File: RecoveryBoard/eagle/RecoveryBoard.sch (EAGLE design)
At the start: 96 parts, among them Q1 BSS123, Q2 BSS123, Q3 BSS123, Q4 BPR-301, Q5 BPR-301, Q6 MOSFET-PCH-SOT23-6, U1 STM32F042K6, U10 TPS63070, U2 BD62120AEFJ-E2, U3 H11F1SR2M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

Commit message: fixed first round of issues with Rev1.0, and fixed some libraries as well
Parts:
- removed U$6: NHQ103B375T10, R--NHQ103B375T10--Thermistor:NHQ103B375T10
- removed U$8: SI7465DP, Q--Si7465DP--Vishay Power MOSFET with multple S+D leads:SI7465DP
- added Q7: SI7465DP-T1-E3, Q--Si7465DP--Vishay Power MOSFET with multple S+D leads:SI7465DP-T1-E3
- added R5: (no value), R--NHQ103B375T10--Thermistor 10K:NHQ103B375T10
- C22: device oresat-rcl:C-EUC1206 -> oresat-rcl:C-EU0805-A-NOSILK
- R8, R9: value 470 -> 220
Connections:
- net +12V: now also Q7.D; no longer U$8.D
- net 3.3V: now also J2.5; no longer J2.3
- net GND: now also J2.1, R5.P$2; no longer J2.5, U$6.P1
- net LAMOTOR+: now also J2.3; no longer J2.1
- net LAMOTOR-: now also J2.4; no longer J2.2
- net N$16: now also Q7.G; no longer U$8.G
- net N$20: now also R5.P$1; no longer U$6.P2
- net POT_OUT_AN: now also J2.2; no longer J2.4
- net VBAT: now also Q7.S; no longer U$8.S
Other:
- note removed: "MOTOR+"
- note removed: "MOTOR-"
- note removed: "POT out"
- note removed: "POT+"
- note removed: "POT-"
- moved on the sheet: JP4

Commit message: updated board with more test points, rearranged LA pins, and rearannged AI STM32 pins
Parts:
- added TP11, TP12, TP13, TP14, TP15, TP16, TP17, TP5, TP7, TP8: TEST-POINT, Tova:TEST-POINT
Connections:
- net IN1 renamed LA_IN1
- net IN2 renamed LA_IN2
- removed net POT_OUT_AN: J2.2, U1.PA10
- new net LA_POS: J2.2, TP8.1, U1.PA1
- net BATT_READ: now also U1.PB1; no longer U1.PB6
- net CHUTE: now also TP13.1
- net DROGUE: now also TP12.1
- net ISO-CHUTE: now also TP14.1
- net ISO-DROGUE: now also TP15.1
- net N$16: now also TP11.1
- net N$2: now also TP16.1
- net N$5: now also TP17.1
- net SENSOR1: now also TP5.1
- net SENSOR2: now also TP7.1
- net SPKR: now also U1.PA10; no longer U1.PB1
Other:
- moved on the sheet: R8, R9

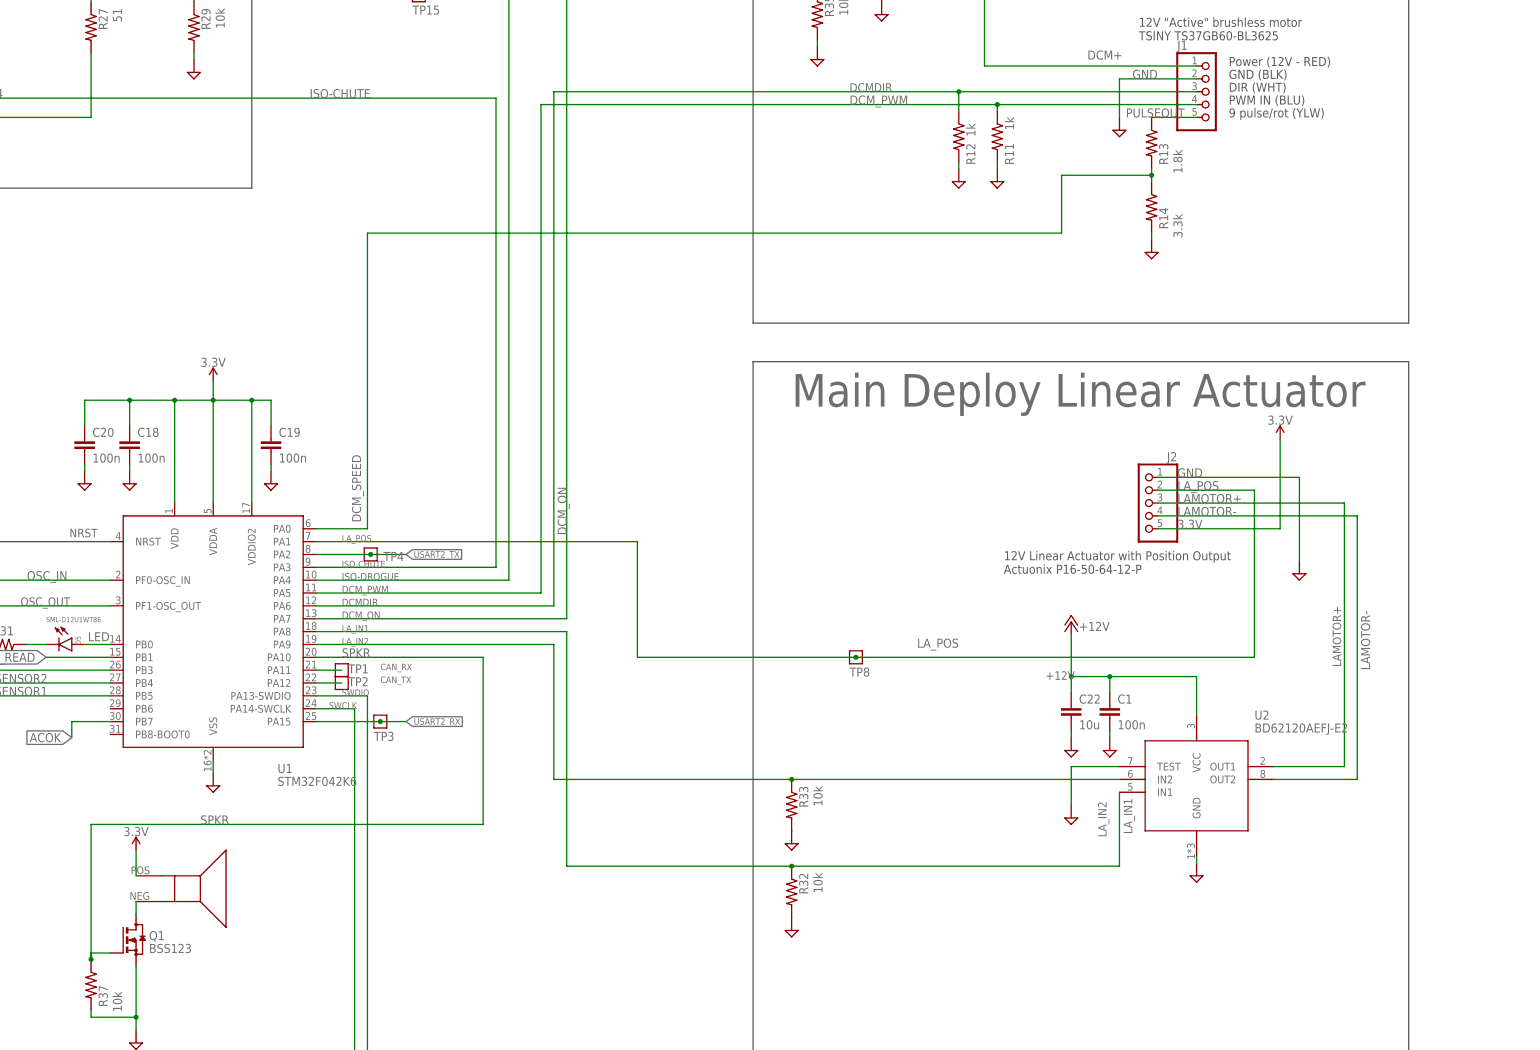
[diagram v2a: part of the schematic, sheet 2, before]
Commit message: finishing routing for REV 2.0
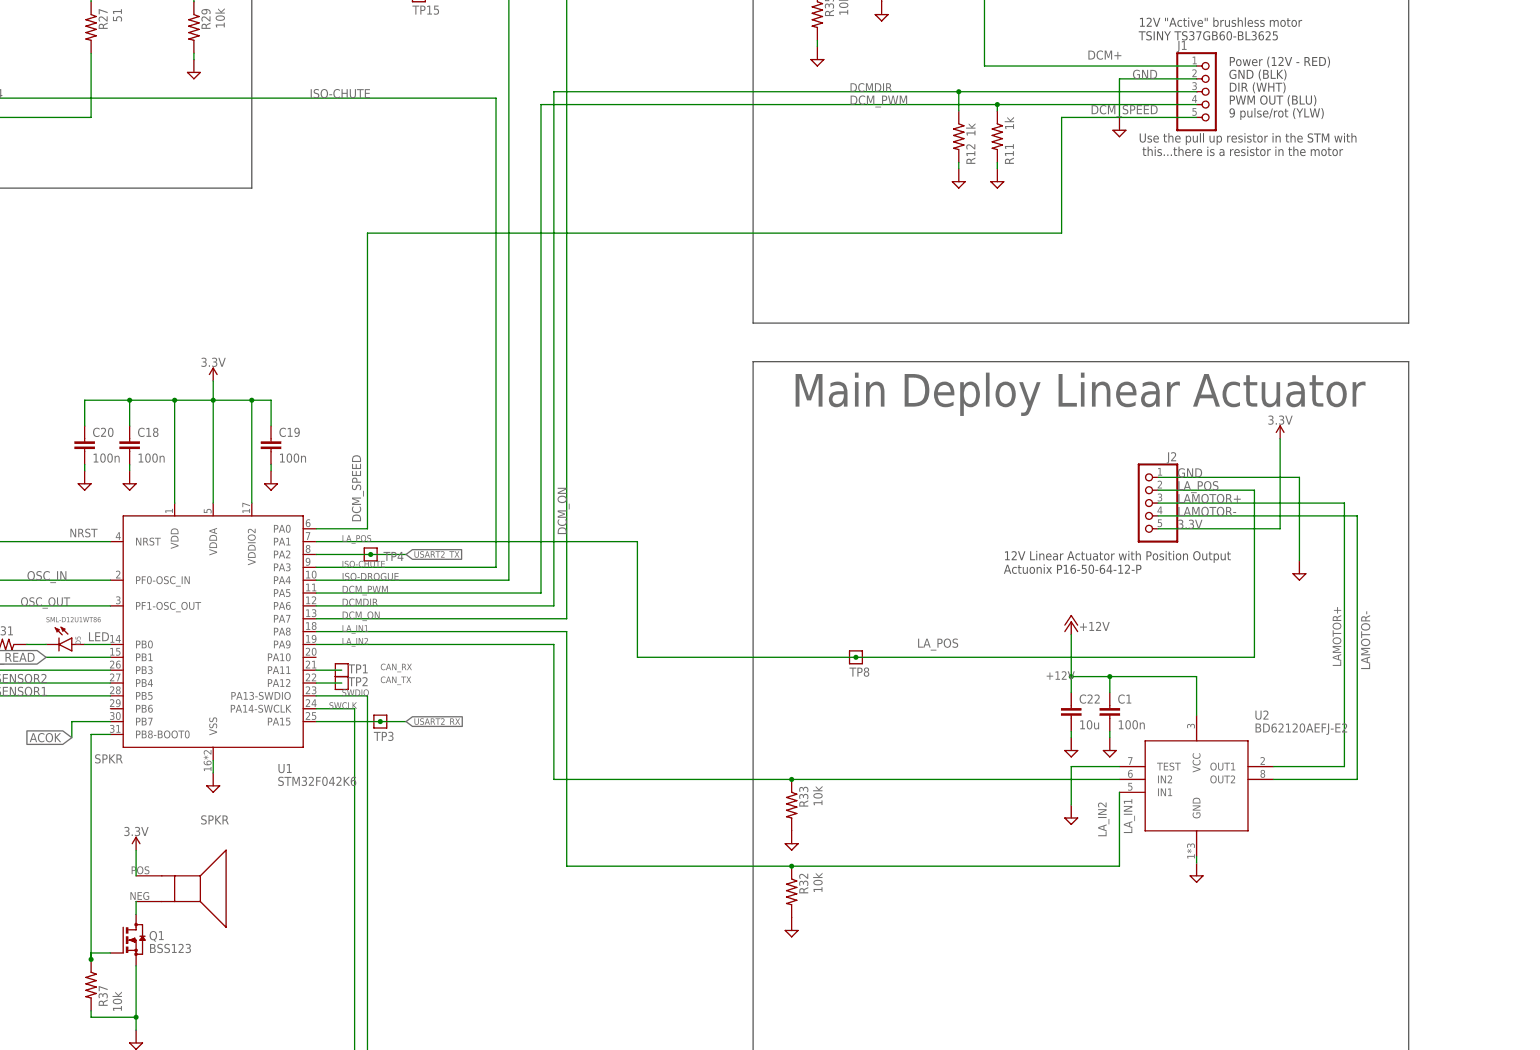
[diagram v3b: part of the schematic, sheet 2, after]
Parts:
- removed R13: 1.8k, oresat-rcl:R-US_0603-C-NOSILK
- removed R14: 3.3k, oresat-rcl:R-US_0603-C-NOSILK
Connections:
- removed net PULSEOUT: J1.5, R13.1
- net DCM_SPEED: now also J1.5; no longer R13.2, R14.1
- net GND: no longer R14.2
- net SPKR: now also U1.PB8-BOOT0; no longer U1.PA10
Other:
- note added: "PWM OUT (BLU)"
- note added: "Use the pull up resistor in the STM with this...there is a resistor in the motor"
- note removed: "PWM IN (BLU)"
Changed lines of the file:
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@@
 <part name="P+1" library="supply1" library_urn="urn:adsk.eagle:library:371" deviceset="+12V" device=""/>
 <part name="SUPPLY38" library="supply2" library_urn="urn:adsk.eagle:library:372" deviceset="GND" device=""/>
-<part name="SUPPLY39" library="supply2" library_urn="urn:adsk.eagle:library:372" deviceset="GND" device=""/>
 <part name="SUPPLY40" library="supply2" library_urn="urn:adsk.eagle:library:372" deviceset="GND" device=""/>
 <part name="SUPPLY41" library="SparkFun-PowerSymbols" library_urn="urn:adsk.eagle:library:530" deviceset="3.3V" device=""/>
@@
 <part name="SUPPLY8" library="supply2" library_urn="urn:adsk.eagle:library:372" deviceset="GND" device=""/>
 <part name="SUPPLY9" library="supply2" library_urn="urn:adsk.eagle:library:372" deviceset="GND" device=""/>
-<part name="R13" library="oresat-rcl" deviceset="R-US_" device="0603-C-NOSILK" value="1.8k"/>
-<part name="R14" library="oresat-rcl" deviceset="R-US_" device="0603-C-NOSILK" value="3.3k"/>
 <part name="P+4" library="supply1" library_urn="urn:adsk.eagle:library:371" deviceset="+12V" device=""/>
 <part name="R15" library="oresat-rcl" deviceset="R-US_" device="0603-C-NOSILK" value="27k">
@@
 <instance part="D1" gate="G$1" x="166.37" y="198.12" smashed="yes">
 <attribute name="NAME" x="163.83" y="200.66" size="1.016" layer="95" ratio="10"/>
-<attribute name="VALUE" x="163.83" y="194.31" size="1.016" layer="96" ratio="10"/>
+<attribute name="VALUE" x="164.465" y="193.675" size="1.016" layer="96" ratio="10"/>
 </instance>
 <instance part="C11" gate="CE" x="148.59" y="195.58" smashed="yes">
@@
 <text x="474.98" y="294.64" size="1.778" layer="97">GND (BLK)</text>
 <text x="474.98" y="292.1" size="1.778" layer="97">DIR (WHT)</text>
-<text x="474.98" y="289.56" size="1.778" layer="97">PWM IN (BLU)</text>
+<text x="474.98" y="289.56" size="1.778" layer="97">PWM OUT (BLU)</text>
 <text x="474.98" y="287.02" size="1.778" layer="97">9 pulse/rot (YLW)</text>
 <text x="137.16" y="367.03" size="6.4516" layer="95">Opto-isolated Inputs
@@
 <wire x1="510.54" y1="96.52" x2="381" y2="96.52" width="0.1524" layer="97"/>
 <wire x1="381" y1="96.52" x2="381" y2="238.76" width="0.1524" layer="97"/>
+<text x="457.2" y="279.4" size="1.778" layer="97">Use the pull up resistor in the STM with
+ this...there is a resistor in the motor</text>
 </plain>
 <instances>
@@
 </instance>
 <instance part="SUPPLY38" gate="GND" x="453.39" y="284.48" smashed="yes"/>
-<instance part="SUPPLY39" gate="GND" x="459.74" y="260.35" smashed="yes"/>
 <instance part="SUPPLY40" gate="GND" x="488.95" y="196.85" smashed="yes"/>
 <instance part="SUPPLY41" gate="G$1" x="485.14" y="223.52" smashed="yes">
@@
 <instance part="SUPPLY8" gate="GND" x="421.64" y="274.32" smashed="yes"/>
 <instance part="SUPPLY9" gate="GND" x="429.26" y="274.32" smashed="yes"/>
-<instance part="R13" gate="R" x="459.74" y="281.94" smashed="yes" rot="R270">
-<attribute name="NAME" x="461.2386" y="281.94" size="1.778" layer="95" rot="R270"/>
-<attribute name="VALUE" x="464.058" y="280.67" size="1.778" layer="96" rot="R270"/>
-</instance>
-<instance part="R14" gate="R" x="459.74" y="269.24" smashed="yes" rot="R270">
-<attribute name="NAME" x="461.2386" y="269.24" size="1.778" layer="95" rot="R270"/>
-<attribute name="VALUE" x="464.058" y="267.97" size="1.778" layer="96" rot="R270"/>
-</instance>
 <instance part="U$7" gate="G$1" x="271.78" y="134.62" smashed="yes"/>
 <instance part="SUPPLY23" gate="GND" x="96.52" y="87.63" smashed="yes"/>
@@
 <pinref part="R11" gate="R" pin="2"/>
 <wire x1="429.26" y1="276.86" x2="429.26" y2="278.13" width="0.1524" layer="91"/>
-</segment>
-<segment>
-<pinref part="R14" gate="R" pin="2"/>
-<pinref part="SUPPLY39" gate="GND" pin="GND"/>
-<wire x1="459.74" y1="264.16" x2="459.74" y2="262.89" width="0.1524" layer="91"/>
 </segment>
 <segment>
@@
 </segment>
 </net>
-<net name="PULSEOUT" class="0">
-<segment>
-<pinref part="J1" gate="A" pin="5"/>
-<wire x1="468.63" y1="287.02" x2="459.74" y2="287.02" width="0.1524" layer="91"/>
-<pinref part="R13" gate="R" pin="1"/>
-<label x="454.66" y="287.02" size="1.778" layer="95"/>
-</segment>
-</net>
-<net name="DCM_SPEED" class="0">
-<segment>
-<pinref part="R14" gate="R" pin="1"/>
-<pinref part="R13" gate="R" pin="2"/>
-<wire x1="441.96" y1="275.59" x2="441.96" y2="264.16" width="0.1524" layer="91"/>
-<wire x1="441.96" y1="264.16" x2="304.8" y2="264.16" width="0.1524" layer="91"/>
-<wire x1="459.74" y1="274.32" x2="459.74" y2="275.59" width="0.1524" layer="91"/>
-<wire x1="459.74" y1="275.59" x2="459.74" y2="276.86" width="0.1524" layer="91"/>
-<wire x1="441.96" y1="275.59" x2="459.74" y2="275.59" width="0.1524" layer="91"/>
-<junction x="459.74" y="275.59"/>
-<pinref part="U1" gate="G$1" pin="PA0"/>
-<label x="303.53" y="207.01" size="1.778" layer="95" rot="R90"/>
-<wire x1="304.8" y1="264.16" x2="304.8" y2="205.74" width="0.1524" layer="91"/>
-<wire x1="304.8" y1="205.74" x2="294.64" y2="205.74" width="0.1524" layer="91"/>
-</segment>
-</net>
 <net name="CAN_RX" class="0">
 <segment>
@@
 <pinref part="R37" gate="R" pin="1"/>
 <wire x1="250.19" y1="120.65" x2="250.19" y2="121.92" width="0.1524" layer="91"/>
-<pinref part="U1" gate="G$1" pin="PA10"/>
-<wire x1="294.64" y1="180.34" x2="327.66" y2="180.34" width="0.1524" layer="91"/>
-<wire x1="327.66" y1="180.34" x2="327.66" y2="147.32" width="0.1524" layer="91"/>
-<wire x1="327.66" y1="147.32" x2="250.19" y2="147.32" width="0.1524" layer="91"/>
-<wire x1="250.19" y1="147.32" x2="250.19" y2="120.65" width="0.1524" layer="91"/>
 <junction x="250.19" y="120.65"/>
-<label x="299.72" y="180.34" size="1.778" layer="95"/>
+<label x="250.825" y="159.385" size="1.778" layer="95"/>
 <label x="271.78" y="147.32" size="1.778" layer="95"/>
+<pinref part="U1" gate="G$1" pin="PB8-BOOT0"/>
+<wire x1="250.19" y1="165.1" x2="250.19" y2="120.65" width="0.1524" layer="91"/>
+<wire x1="254" y1="165.1" x2="250.19" y2="165.1" width="0.1524" layer="91"/>
 </segment>
 </net>
@@
 </segment>
 </net>
+<net name="DCM_SPEED" class="0">
+<segment>
+<pinref part="J1" gate="A" pin="5"/>
+<label x="447.675" y="287.655" size="1.778" layer="95"/>
+<wire x1="441.96" y1="264.16" x2="304.8" y2="264.16" width="0.1524" layer="91"/>
+<pinref part="U1" gate="G$1" pin="PA0"/>
+<label x="303.53" y="207.01" size="1.778" layer="95" rot="R90"/>
+<wire x1="304.8" y1="264.16" x2="304.8" y2="205.74" width="0.1524" layer="91"/>
+<wire x1="304.8" y1="205.74" x2="294.64" y2="205.74" width="0.1524" layer="91"/>
+<wire x1="468.63" y1="287.02" x2="441.96" y2="287.02" width="0.1524" layer="91"/>
+<wire x1="441.96" y1="287.02" x2="441.96" y2="264.16" width="0.1524" layer="91"/>
+</segment>
+</net>
